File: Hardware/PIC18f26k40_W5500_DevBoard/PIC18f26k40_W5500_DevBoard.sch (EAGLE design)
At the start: 37 parts, among them J2 MAGJACK, U1 W5500, U2 PIC18F2523-I/SO

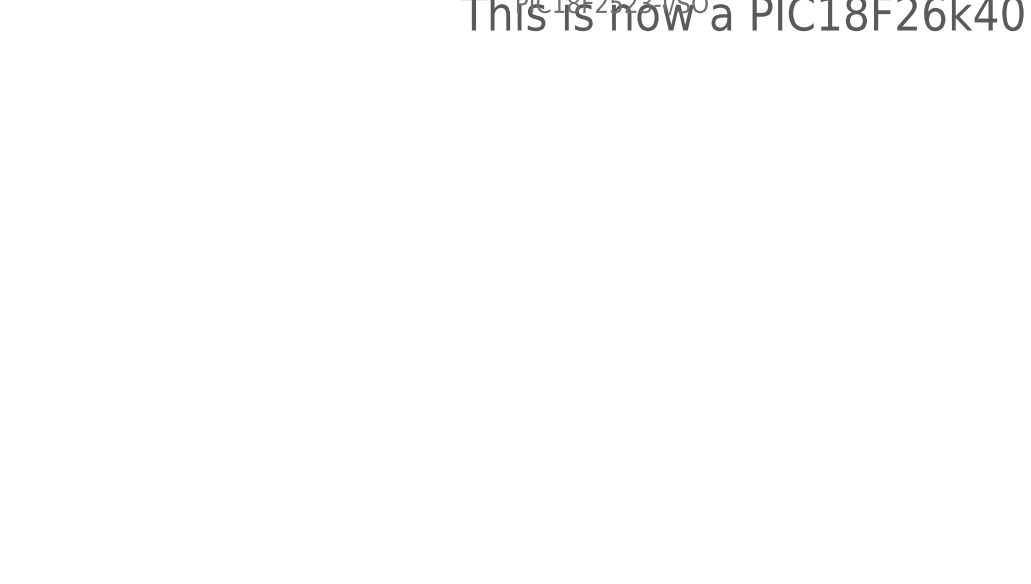
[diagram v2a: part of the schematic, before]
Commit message: Connected every PIC pin to a header
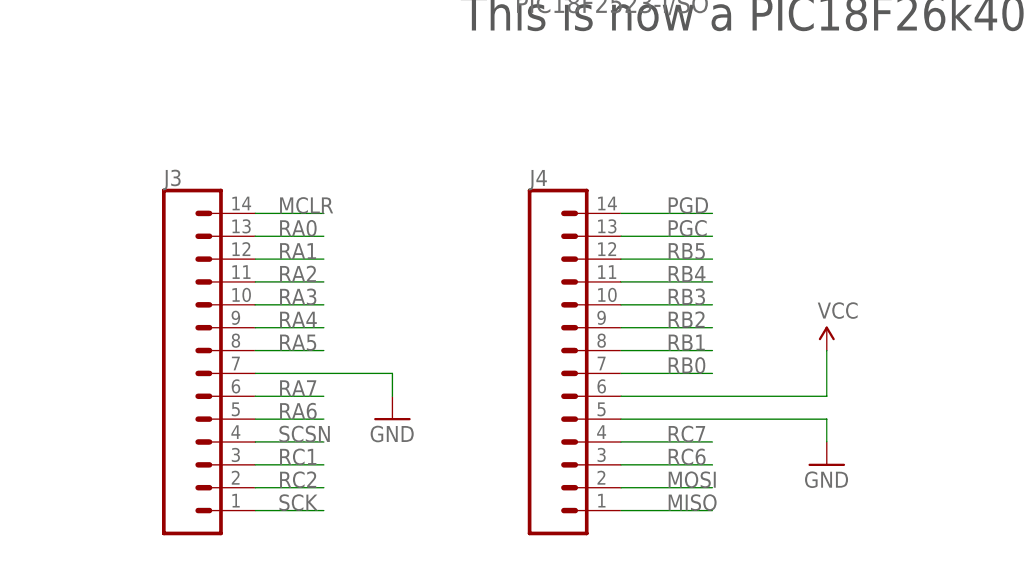
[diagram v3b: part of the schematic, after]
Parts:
- added J3, J4: (no value), SparkFun-Connectors:CONN_14
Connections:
- net GND: now also J3.7, J4.5
- net MCLR: now also J3.14
- net MISO: now also J4.1
- net MOSI: now also J4.2
- net PGC: now also J4.13
- net PGD: now also J4.14
- net RA0: now also J3.13
- net RA1: now also J3.12
- net RA2: now also J3.11
- net RA3: now also J3.10
- net RA4: now also J3.9
- net RA5: now also J3.8
- net RA6: now also J3.5
- net RA7: now also J3.6
- net RB0: now also J4.7
- net RB1: now also J4.8
- net RB2: now also J4.9
- net RB3: now also J4.10
- net RB4: now also J4.11
- net RB5: now also J4.12
- net RC1: now also J3.3
- net RC2: now also J3.2
- net RC6: now also J4.3
- net RC7: now also J4.4
- net SCK: now also J3.1
- net SCSN: now also J3.4
- net VCC: now also J4.6
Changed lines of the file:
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@@
 <part name="R11" library="SparkFun-Passives" deviceset="RESISTOR" device="0603-RES" value="51"/>
 <part name="GND14" library="SparkFun-Aesthetics" deviceset="GND" device=""/>
+<part name="J3" library="SparkFun-Connectors" deviceset="CONN_14" device=""/>
+<part name="J4" library="SparkFun-Connectors" deviceset="CONN_14" device=""/>
+<part name="GND15" library="SparkFun-Aesthetics" deviceset="GND" device=""/>
+<part name="GND16" library="SparkFun-Aesthetics" deviceset="GND" device=""/>
+<part name="SUPPLY11" library="SparkFun-Aesthetics" deviceset="VCC" device=""/>
 </parts>
 <sheets>
@@
 <instance part="R11" gate="G$1" x="187.96" y="-17.78" rot="R90"/>
 <instance part="GND14" gate="1" x="190.5" y="-38.1"/>
+<instance part="J3" gate="G$1" x="7.62" y="-17.78"/>
+<instance part="J4" gate="G$1" x="48.26" y="-17.78"/>
+<instance part="GND15" gate="1" x="33.02" y="-25.4"/>
+<instance part="GND16" gate="1" x="81.28" y="-30.48"/>
+<instance part="SUPPLY11" gate="G$1" x="81.28" y="-17.78"/>
 </instances>
 <busses>
@@
 <label x="238.76" y="99.06" size="1.778" layer="95"/>
 </segment>
+<segment>
+<pinref part="J4" gate="G$1" pin="2"/>
+<wire x1="58.42" y1="-33.02" x2="68.58" y2="-33.02" width="0.1524" layer="91"/>
+<label x="63.5" y="-33.02" size="1.778" layer="95"/>
+</segment>
 </net>
 <net name="MISO" class="0">
@@
 <label x="238.76" y="96.52" size="1.778" layer="95"/>
 </segment>
+<segment>
+<pinref part="J4" gate="G$1" pin="1"/>
+<wire x1="58.42" y1="-35.56" x2="68.58" y2="-35.56" width="0.1524" layer="91"/>
+<label x="63.5" y="-35.56" size="1.778" layer="95"/>
+</segment>
 </net>
 <net name="SCK" class="0">
@@
 <wire x1="236.22" y1="93.98" x2="246.38" y2="93.98" width="0.1524" layer="91"/>
 <label x="238.76" y="93.98" size="1.778" layer="95"/>
+</segment>
+<segment>
+<pinref part="J3" gate="G$1" pin="1"/>
+<wire x1="17.78" y1="-35.56" x2="25.4" y2="-35.56" width="0.1524" layer="91"/>
+<label x="20.32" y="-35.56" size="1.778" layer="95"/>
 </segment>
 </net>
@@
 <wire x1="264.16" y1="91.44" x2="264.16" y2="104.14" width="0.1524" layer="91"/>
 <pinref part="R4" gate="G$1" pin="1"/>
+</segment>
+<segment>
+<pinref part="J3" gate="G$1" pin="4"/>
+<wire x1="17.78" y1="-27.94" x2="25.4" y2="-27.94" width="0.1524" layer="91"/>
+<label x="20.32" y="-27.94" size="1.778" layer="95"/>
 </segment>
 </net>
@@
 <junction x="297.18" y="7.62"/>
 <pinref part="SUPPLY10" gate="G$1" pin="VCC"/>
+</segment>
+<segment>
+<pinref part="J4" gate="G$1" pin="6"/>
+<wire x1="58.42" y1="-22.86" x2="81.28" y2="-22.86" width="0.1524" layer="91"/>
+<wire x1="81.28" y1="-22.86" x2="81.28" y2="-17.78" width="0.1524" layer="91"/>
+<pinref part="SUPPLY11" gate="G$1" pin="VCC"/>
 </segment>
 </net>
@@
 <pinref part="GND14" gate="1" pin="GND"/>
 <wire x1="190.5" y1="-33.02" x2="190.5" y2="-35.56" width="0.1524" layer="91"/>
+</segment>
+<segment>
+<pinref part="J3" gate="G$1" pin="7"/>
+<wire x1="17.78" y1="-20.32" x2="33.02" y2="-20.32" width="0.1524" layer="91"/>
+<wire x1="33.02" y1="-20.32" x2="33.02" y2="-22.86" width="0.1524" layer="91"/>
+<pinref part="GND15" gate="1" pin="GND"/>
+</segment>
+<segment>
+<pinref part="J4" gate="G$1" pin="5"/>
+<wire x1="58.42" y1="-25.4" x2="81.28" y2="-25.4" width="0.1524" layer="91"/>
+<wire x1="81.28" y1="-25.4" x2="81.28" y2="-27.94" width="0.1524" layer="91"/>
+<pinref part="GND16" gate="1" pin="GND"/>
 </segment>
 </net>
@@
 <label x="-30.48" y="83.82" size="1.778" layer="95"/>
 </segment>
+<segment>
+<pinref part="J3" gate="G$1" pin="14"/>
+<wire x1="17.78" y1="-2.54" x2="25.4" y2="-2.54" width="0.1524" layer="91"/>
+<label x="20.32" y="-2.54" size="1.778" layer="95"/>
+</segment>
 </net>
 <net name="PGD" class="0">
@@
 <label x="-25.4" y="38.1" size="1.778" layer="95"/>
 </segment>
+<segment>
+<pinref part="J4" gate="G$1" pin="14"/>
+<wire x1="58.42" y1="-2.54" x2="68.58" y2="-2.54" width="0.1524" layer="91"/>
+<label x="63.5" y="-2.54" size="1.778" layer="95"/>
+</segment>
 </net>
 <net name="PGC" class="0">
@@
 <wire x1="-10.16" y1="40.64" x2="-27.94" y2="40.64" width="0.1524" layer="91"/>
 <label x="-25.4" y="40.64" size="1.778" layer="95"/>
+</segment>
+<segment>
+<pinref part="J4" gate="G$1" pin="13"/>
+<wire x1="58.42" y1="-5.08" x2="68.58" y2="-5.08" width="0.1524" layer="91"/>
+<label x="63.5" y="-5.08" size="1.778" layer="95"/>
 </segment>
 </net>
@@
 <label x="127" y="86.36" size="1.778" layer="95"/>
 </segment>
+<segment>
+<pinref part="J3" gate="G$1" pin="3"/>
+<wire x1="17.78" y1="-30.48" x2="25.4" y2="-30.48" width="0.1524" layer="91"/>
+<label x="20.32" y="-30.48" size="1.778" layer="95"/>
+</segment>
 </net>
 <net name="RC2" class="0">
@@
 <label x="127" y="83.82" size="1.778" layer="95"/>
 </segment>
+<segment>
+<pinref part="J3" gate="G$1" pin="2"/>
+<wire x1="17.78" y1="-33.02" x2="25.4" y2="-33.02" width="0.1524" layer="91"/>
+<label x="20.32" y="-33.02" size="1.778" layer="95"/>
+</segment>
 </net>
 <net name="RC6" class="0">
@@
 <label x="124.46" y="73.66" size="1.778" layer="95"/>
 </segment>
+<segment>
+<pinref part="J4" gate="G$1" pin="3"/>
+<wire x1="58.42" y1="-30.48" x2="68.58" y2="-30.48" width="0.1524" layer="91"/>
+<label x="63.5" y="-30.48" size="1.778" layer="95"/>
+</segment>
 </net>
 <net name="RC7" class="0">
@@
 <label x="124.46" y="71.12" size="1.778" layer="95"/>
 </segment>
+<segment>
+<pinref part="J4" gate="G$1" pin="4"/>
+<wire x1="58.42" y1="-27.94" x2="68.58" y2="-27.94" width="0.1524" layer="91"/>
+<label x="63.5" y="-27.94" size="1.778" layer="95"/>
+</segment>
 </net>
 <net name="RA0" class="0">
@@
 <label x="-33.02" y="78.74" size="1.778" layer="95"/>
 </segment>
+<segment>
+<pinref part="J3" gate="G$1" pin="13"/>
+<wire x1="17.78" y1="-5.08" x2="25.4" y2="-5.08" width="0.1524" layer="91"/>
+<label x="20.32" y="-5.08" size="1.778" layer="95"/>
+</segment>
 </net>
 <net name="RA1" class="0">
@@
 <label x="-33.02" y="76.2" size="1.778" layer="95"/>
 </segment>
+<segment>
+<pinref part="J3" gate="G$1" pin="12"/>
+<wire x1="17.78" y1="-7.62" x2="25.4" y2="-7.62" width="0.1524" layer="91"/>
+<label x="20.32" y="-7.62" size="1.778" layer="95"/>
+</segment>
 </net>
 <net name="RA2" class="0">
@@
 <label x="-33.02" y="73.66" size="1.778" layer="95"/>
 </segment>
+<segment>
+<pinref part="J3" gate="G$1" pin="11"/>
+<wire x1="17.78" y1="-10.16" x2="25.4" y2="-10.16" width="0.1524" layer="91"/>
+<label x="20.32" y="-10.16" size="1.778" layer="95"/>
+</segment>
 </net>
 <net name="RA3" class="0">
@@
 <label x="-33.02" y="71.12" size="1.778" layer="95"/>
 </segment>
+<segment>
+<pinref part="J3" gate="G$1" pin="10"/>
+<wire x1="17.78" y1="-12.7" x2="25.4" y2="-12.7" width="0.1524" layer="91"/>
+<label x="20.32" y="-12.7" size="1.778" layer="95"/>
+</segment>
 </net>
 <net name="RA4" class="0">
@@
 <label x="-33.02" y="68.58" size="1.778" layer="95"/>
 </segment>
+<segment>
+<pinref part="J3" gate="G$1" pin="9"/>
+<wire x1="17.78" y1="-15.24" x2="25.4" y2="-15.24" width="0.1524" layer="91"/>
+<label x="20.32" y="-15.24" size="1.778" layer="95"/>
+</segment>
 </net>
 <net name="RA5" class="0">
@@
 <label x="-33.02" y="66.04" size="1.778" layer="95"/>
 </segment>
+<segment>
+<pinref part="J3" gate="G$1" pin="8"/>
+<wire x1="17.78" y1="-17.78" x2="25.4" y2="-17.78" width="0.1524" layer="91"/>
+<label x="20.32" y="-17.78" size="1.778" layer="95"/>
+</segment>
 </net>
 <net name="RA6" class="0">
@@
 <label x="-33.02" y="63.5" size="1.778" layer="95"/>
 </segment>
+<segment>
+<pinref part="J3" gate="G$1" pin="5"/>
+<wire x1="17.78" y1="-25.4" x2="25.4" y2="-25.4" width="0.1524" layer="91"/>
+<label x="20.32" y="-25.4" size="1.778" layer="95"/>
+</segment>
 </net>
 <net name="RA7" class="0">
@@
 <label x="-33.02" y="60.96" size="1.778" layer="95"/>
 </segment>
+<segment>
+<pinref part="J3" gate="G$1" pin="6"/>
+<wire x1="17.78" y1="-22.86" x2="25.4" y2="-22.86" width="0.1524" layer="91"/>
+<label x="20.32" y="-22.86" size="1.778" layer="95"/>
+</segment>
 </net>
 <net name="RB0" class="0">
@@
 <label x="-33.02" y="55.88" size="1.778" layer="95"/>
 </segment>
+<segment>
+<pinref part="J4" gate="G$1" pin="7"/>
+<wire x1="58.42" y1="-20.32" x2="68.58" y2="-20.32" width="0.1524" layer="91"/>
+<label x="63.5" y="-20.32" size="1.778" layer="95"/>
+</segment>
 </net>
 <net name="RB1" class="0">
@@
 <label x="-33.02" y="53.34" size="1.778" layer="95"/>
 </segment>
+<segment>
+<pinref part="J4" gate="G$1" pin="8"/>
+<wire x1="58.42" y1="-17.78" x2="68.58" y2="-17.78" width="0.1524" layer="91"/>
+<label x="63.5" y="-17.78" size="1.778" layer="95"/>
+</segment>
 </net>
 <net name="RB2" class="0">
@@
 <label x="-33.02" y="50.8" size="1.778" layer="95"/>
 </segment>
+<segment>
+<pinref part="J4" gate="G$1" pin="9"/>
+<wire x1="58.42" y1="-15.24" x2="68.58" y2="-15.24" width="0.1524" layer="91"/>
+<label x="63.5" y="-15.24" size="1.778" layer="95"/>
+</segment>
 </net>
 <net name="RB3" class="0">
@@
 <label x="-33.02" y="48.26" size="1.778" layer="95"/>
 </segment>
+<segment>
+<pinref part="J4" gate="G$1" pin="10"/>
+<wire x1="58.42" y1="-12.7" x2="68.58" y2="-12.7" width="0.1524" layer="91"/>
+<label x="63.5" y="-12.7" size="1.778" layer="95"/>
+</segment>
 </net>
 <net name="RB4" class="0">
@@
 <label x="-33.02" y="45.72" size="1.778" layer="95"/>
 </segment>
+<segment>
+<pinref part="J4" gate="G$1" pin="11"/>
+<wire x1="58.42" y1="-10.16" x2="68.58" y2="-10.16" width="0.1524" layer="91"/>
+<label x="63.5" y="-10.16" size="1.778" layer="95"/>
+</segment>
 </net>
 <net name="RB5" class="0">
@@
 <label x="-33.02" y="43.18" size="1.778" layer="95"/>
 </segment>
-</net>
+<segment>
+<pinref part="J4" gate="G$1" pin="12"/>
+<wire x1="58.42" y1="-7.62" x2="68.58" y2="-7.62" width="0.1524" layer="91"/>
+<label x="63.5" y="-7.62" size="1.778" layer="95"/>
+</segment>
+</net>
